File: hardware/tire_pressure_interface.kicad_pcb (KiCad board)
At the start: 4 copper layers, 60.3 x 60.4 mm, 81 parts, among them IC1 TPS54202HDDCR, J3 FTSH-107-01-L-D-K, J4 Conn_02x02_Counter_Clockwise, J5 Micro_SD_Card_Det1, Q1 SI2347DS-T1-GE3, T1 TP_+3V3, T10 TP_+5V, T11 TP_+5V, T3 TP_VCC, T8 TP_VCC, T9 TP_+3V3, U1 STM32G0C1KCTxN, U2 LM1117-3.3, U3 XIAO-ESP32-S3-DIP, U7 ADM3057ExRW

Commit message: fixed routing issues
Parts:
- moved C34 34.5 mm to (94.5, 90.6), turned to 90 degrees
- moved C32 32.1 mm to (125.4, 90.0), turned to 90 degrees
- moved FB5 28.7 mm to (98.0, 91.7), turned to 0 degrees
- moved C45 27.9 mm to (124.2, 86.0), turned to 90 degrees
- moved FB3 26.8 mm to (98.0, 89.4), turned to 0 degrees
- moved FB1 24.2 mm to (121.6, 88.9), turned to 0 degrees
- moved FB2 22.1 mm to (121.2, 86.9), turned to 0 degrees
- moved C41 21.6 mm to (101.4, 90.6), turned to 90 degrees
- moved C39 20.0 mm to (100.4, 85.7), turned to -90 degrees
- moved C33 18.9 mm to (118.1, 90.0), turned to 90 degrees
- moved R15 18.0 mm to (102.4, 80.3), turned to -90 degrees
- moved C66 16.5 mm to (109.9, 76.3), turned to 180 degrees
- moved C40 15.8 mm to (102.6, 85.7), turned to 90 degrees
- moved C46 15.6 mm to (118.1, 86.0), turned to 90 degrees
- moved REF** 12.7 mm to (124.6, 128.7)
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- renumbered D3 to ERR, D1 to OK, D2 to WRN
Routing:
- net /Connectors/CAN_P: track 75.9 -> 20.0 mm
- net /Connectors/CAN_N: track 74.5 -> 20.3 mm
- net /CAN_BUS/GND_CAN_ISO1: track 67.5 -> 22.5 mm
- net /CAN_BUS/CAN_TX: track 25.1 -> 44.1 mm
- net /CAN_BUS/STBY_CAN_1: track 24.7 -> 43.7 mm
- net +5V: track 41.4 -> 59.5 mm, vias 0 -> 2
- net /CAN_BUS/CAN_RX: track 29.2 -> 45.4 mm
- net /STM32/LED.OK: track 40.4 -> 30.3 mm
- net /STM32/LED.WRN: track 39.0 -> 29.6 mm
- net Net-(IC1-FB): track 4.73 -> 11.4 mm, vias 0 -> 2
- net /Power/VO_+3.3V: track 6.40 -> 12.1 mm
- net Net-(IC1-BOOT): track 7.71 -> 3.86 mm, vias 2 -> 0
- net /STM32/LED.ACT: track 21.4 -> 18.0 mm
- net GND: track 74.8 -> 78.1 mm, vias 38 -> 40
- net Net-(IC1-SW): track 11.3 -> 14.4 mm
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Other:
- board text added: "ACT"
- board text removed: "D4"

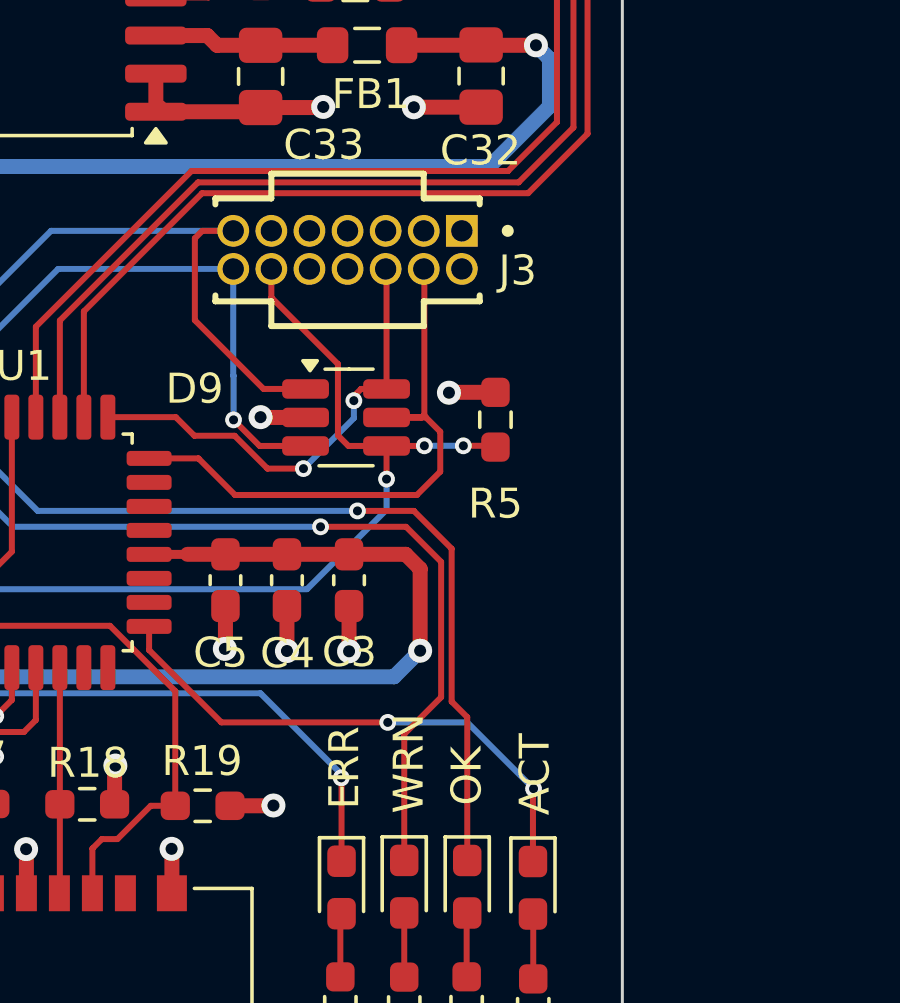
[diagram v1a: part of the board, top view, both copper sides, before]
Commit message: added missing TVS diode
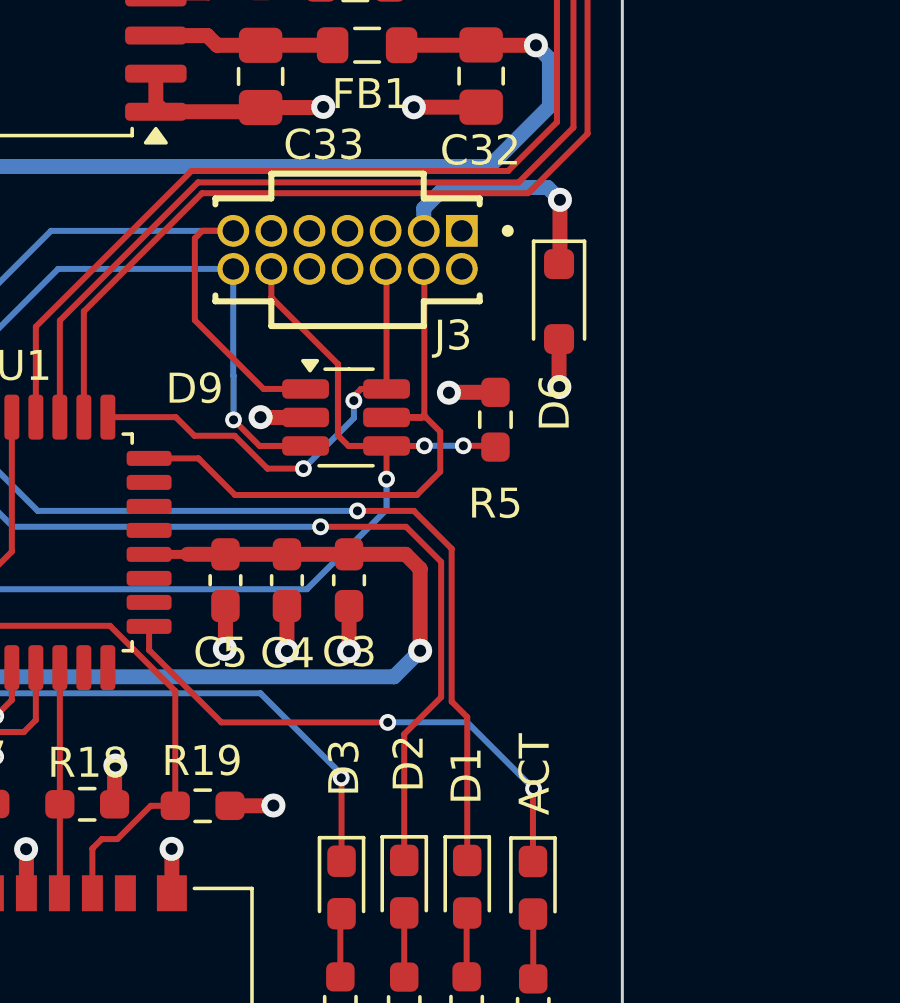
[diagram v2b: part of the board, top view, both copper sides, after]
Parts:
- added D6: PTVS5V0Z1USK, Diode_SMD:D_SOD-323_HandSoldering, F.Cu at (128.0, 97.5)
- renumbered OK to D1, WRN to D2, ERR to D3
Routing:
- net +3V3: track 28.4 -> 36.4 mm, vias 16 -> 17
- net GND: track 78.1 -> 79.7 mm, vias 40 -> 41

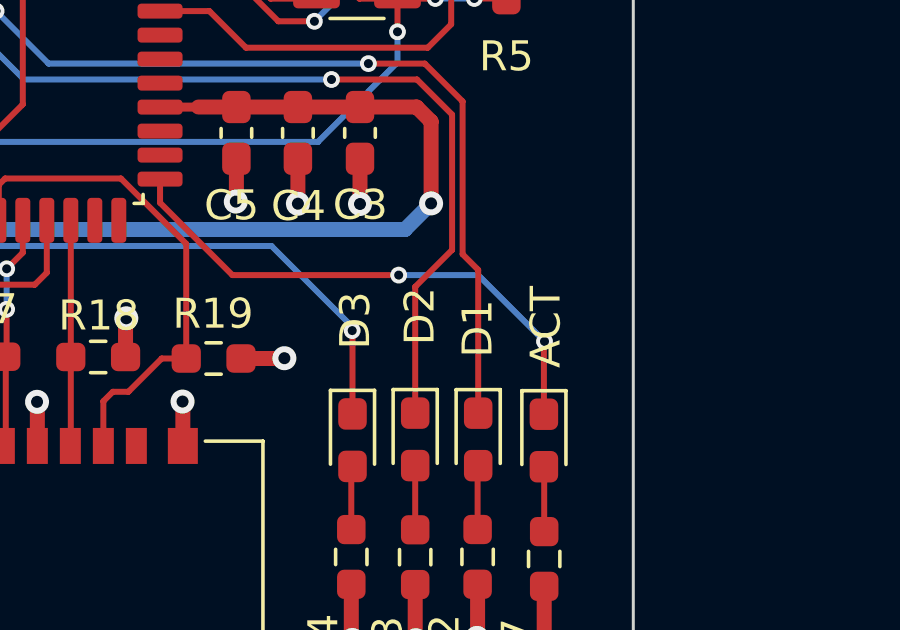
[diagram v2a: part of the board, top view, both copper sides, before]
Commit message: added led description
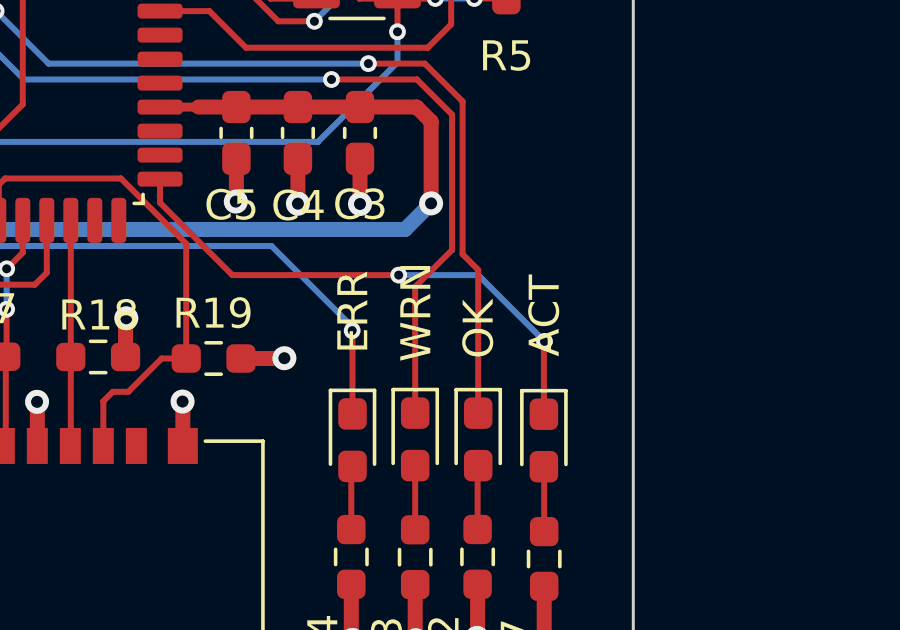
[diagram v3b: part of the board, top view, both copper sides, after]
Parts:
- D6: value PTVS5V0Z1USK -> UCLAMP3301D.TCT
- renumbered D3 to ERR, D1 to OK, D2 to WRN
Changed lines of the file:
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@@
 		(descr "LED SMD 0603 (1608 Metric), square (rectangular) end terminal, IPC-7351 nominal, (Body size source: http://www.tortai-tech.com/upload/download/2011102023233369053.pdf)")
 		(tags "LED handsolder")
-		(property "Reference" "D2"
-			(at -4.105 -0.15 90)
+		(property "Reference" "WRN"
+			(at -4.245 -0.04 90)
 			(layer "F.SilkS")
 			(effects
@@
 			)
 		)
-		(property "Value" "PTVS5V0Z1USK"
+		(property "Value" "UCLAMP3301D.TCT"
 			(at 0.1 1.9 90)
 			(layer "F.Fab")
@@
 		(descr "LED SMD 0603 (1608 Metric), square (rectangular) end terminal, IPC-7351 nominal, (Body size source: http://www.tortai-tech.com/upload/download/2011102023233369053.pdf)")
 		(tags "LED handsolder")
-		(property "Reference" "D3"
-			(at -3.9925 -0.09 90)
+		(property "Reference" "ERR"
+			(at -4.2725 -0.03 90)
 			(layer "F.SilkS")
 			(effects
@@
 		(descr "LED SMD 0603 (1608 Metric), square (rectangular) end terminal, IPC-7351 nominal, (Body size source: http://www.tortai-tech.com/upload/download/2011102023233369053.pdf)")
 		(tags "LED handsolder")
-		(property "Reference" "D1"
-			(at -3.6975 0.02 90)
+		(property "Reference" "OK"
+			(at -3.6775 -0.02 90)
 			(layer "F.SilkS")
 			(effects
@@
 	)
 	(gr_text "ACT"
-		(at 127.22 113.25 90)
+		(at 127.19 112.87 90)
 		(layer "F.SilkS")
 		(effects

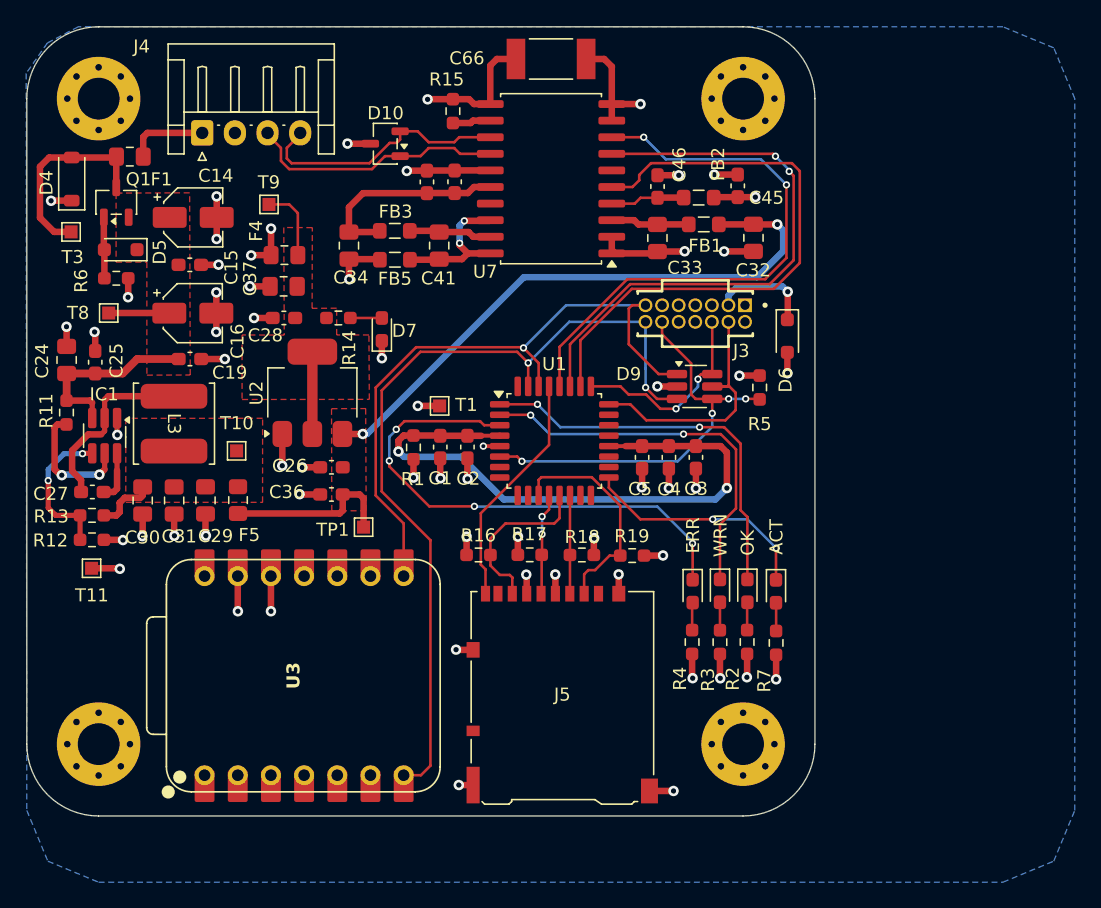
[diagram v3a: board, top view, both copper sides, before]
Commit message: removed 3v3 bcu fill
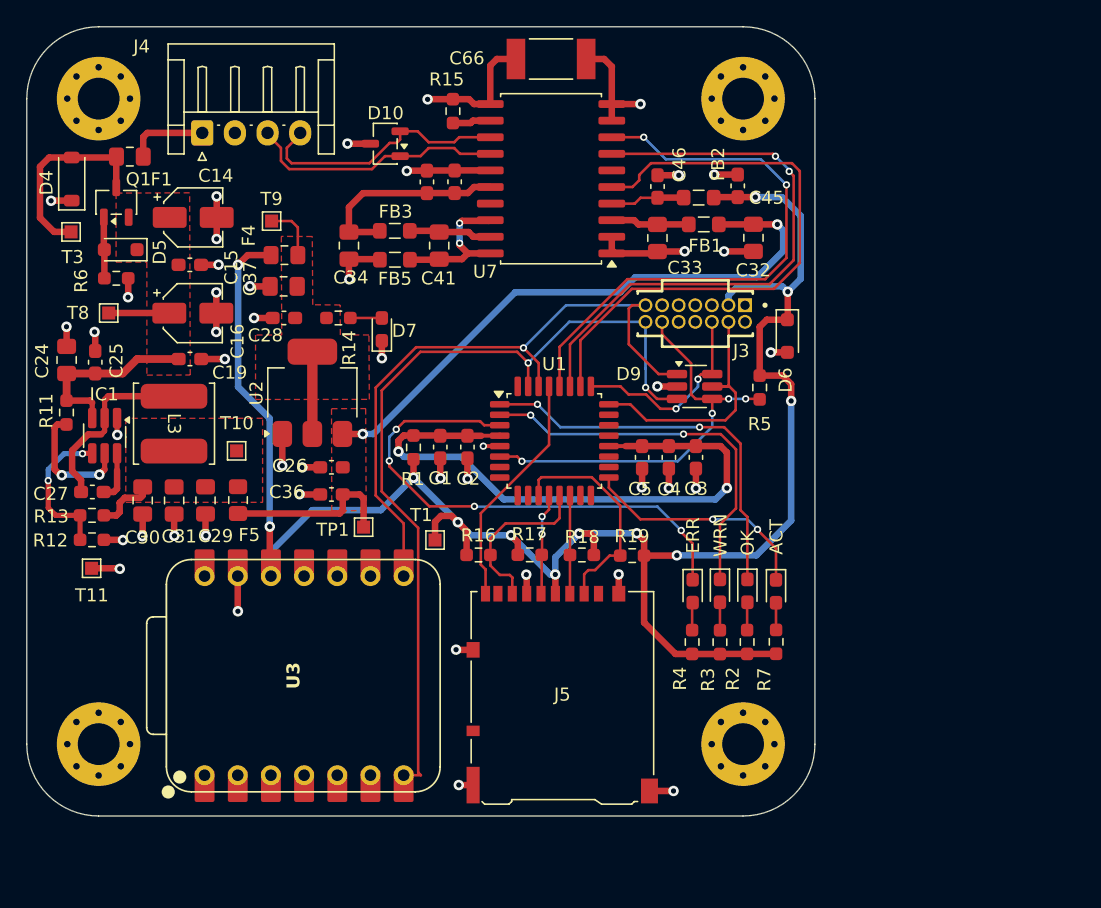
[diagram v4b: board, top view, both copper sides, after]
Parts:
- moved T1 10.3 mm to (101.1, 113.1)
- moved T9 1.29 mm to (88.5, 88.7)
- moved R7 0.08 mm to (127.2, 120.9)
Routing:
- net +3V3: track 36.4 -> 149.0 mm, vias 17 -> 12
- net /Power/VO_+3.3V: track 12.1 -> 10.7 mm
- net /TX: track 65.3 -> 64.7 mm
- removed copper zone on B.Cu, net +3V3

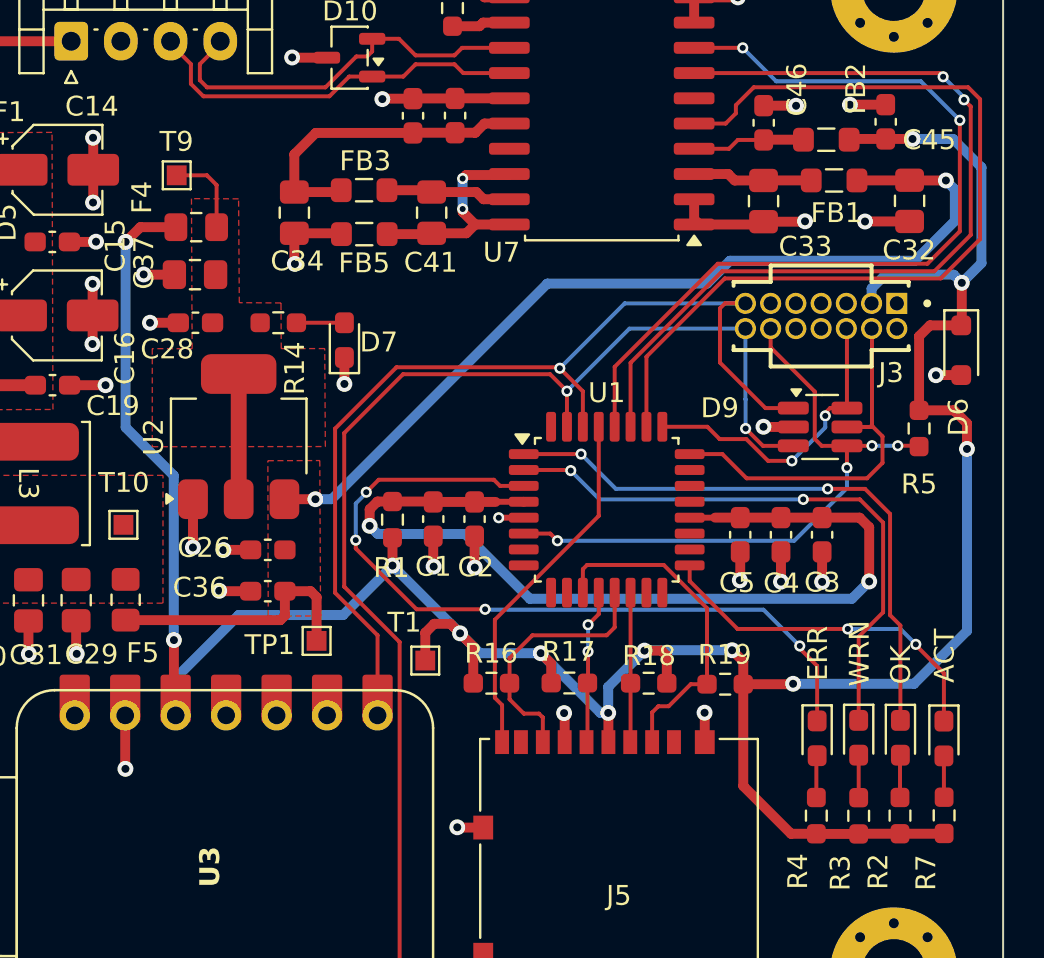
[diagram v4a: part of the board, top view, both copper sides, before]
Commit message: improved 3V3 routing
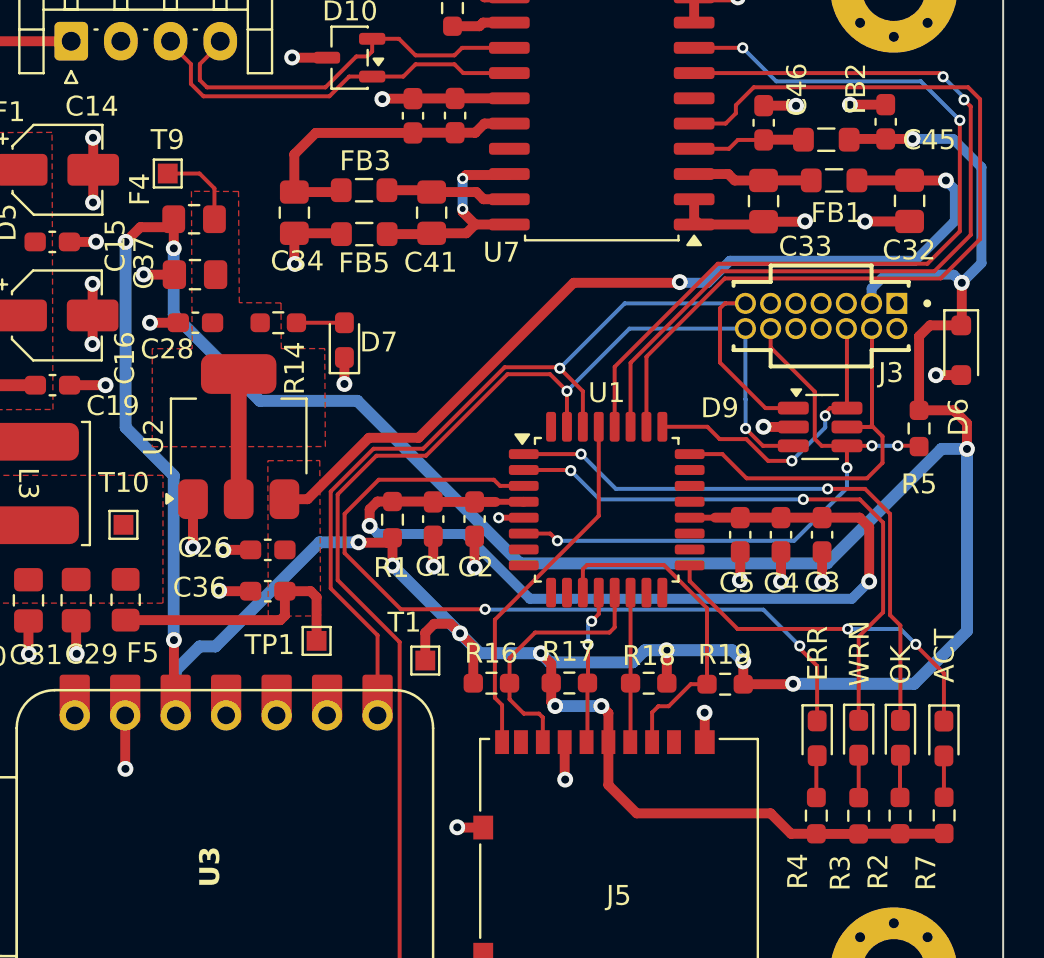
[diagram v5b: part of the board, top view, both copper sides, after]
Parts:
- moved T9 0.46 mm to (88.1, 88.6)
- moved F4 0.41 mm to (89.4, 90.9)
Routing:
- net +3V3: track 149.0 -> 206.3 mm, vias 12 -> 15
- net /RX: track 50.4 -> 48.9 mm
- net /TX: track 64.7 -> 63.3 mm
- net /STM32/LED.ERR: track 39.9 -> 40.8 mm, vias 4 -> 2
